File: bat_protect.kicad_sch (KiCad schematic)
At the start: 17 parts, among them Q6 Q_NMOS_DGS, Q7 Q_NMOS_DGS, Q8 Q_NMOS_DGS, U16 BQ29209DRBR

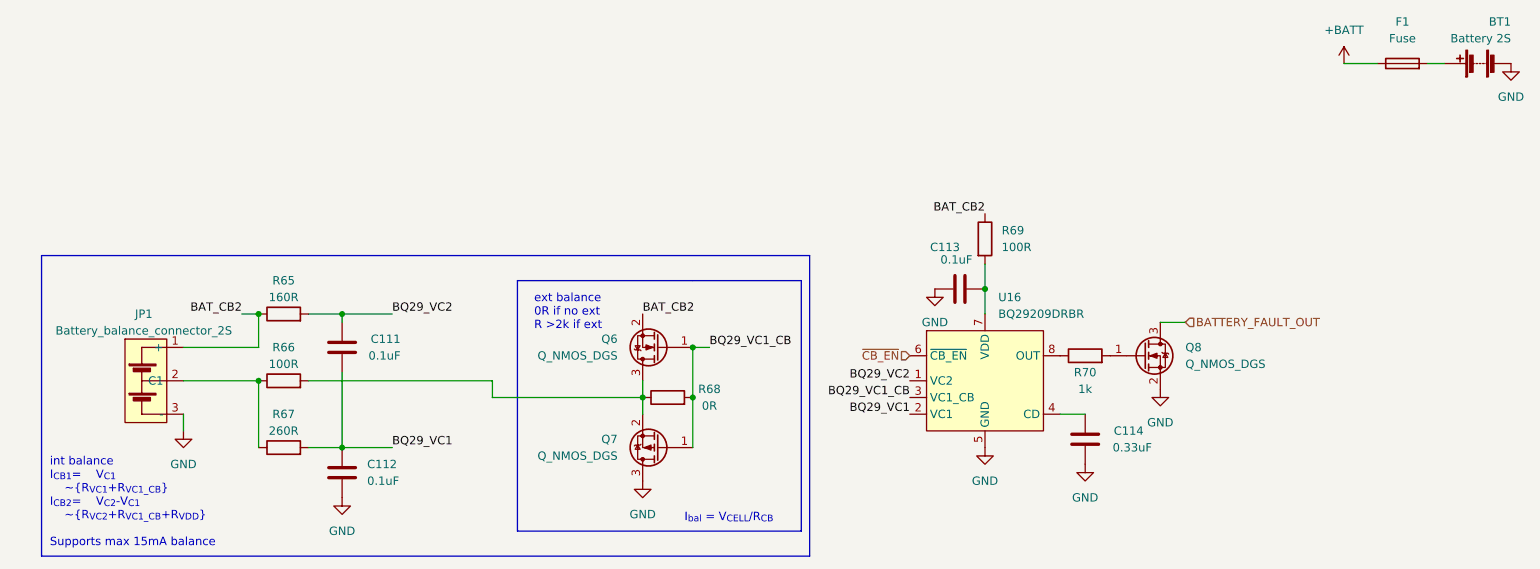
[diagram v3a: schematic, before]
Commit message: copied own LED footprint, modified silkscreen, minor visual changes in schematics
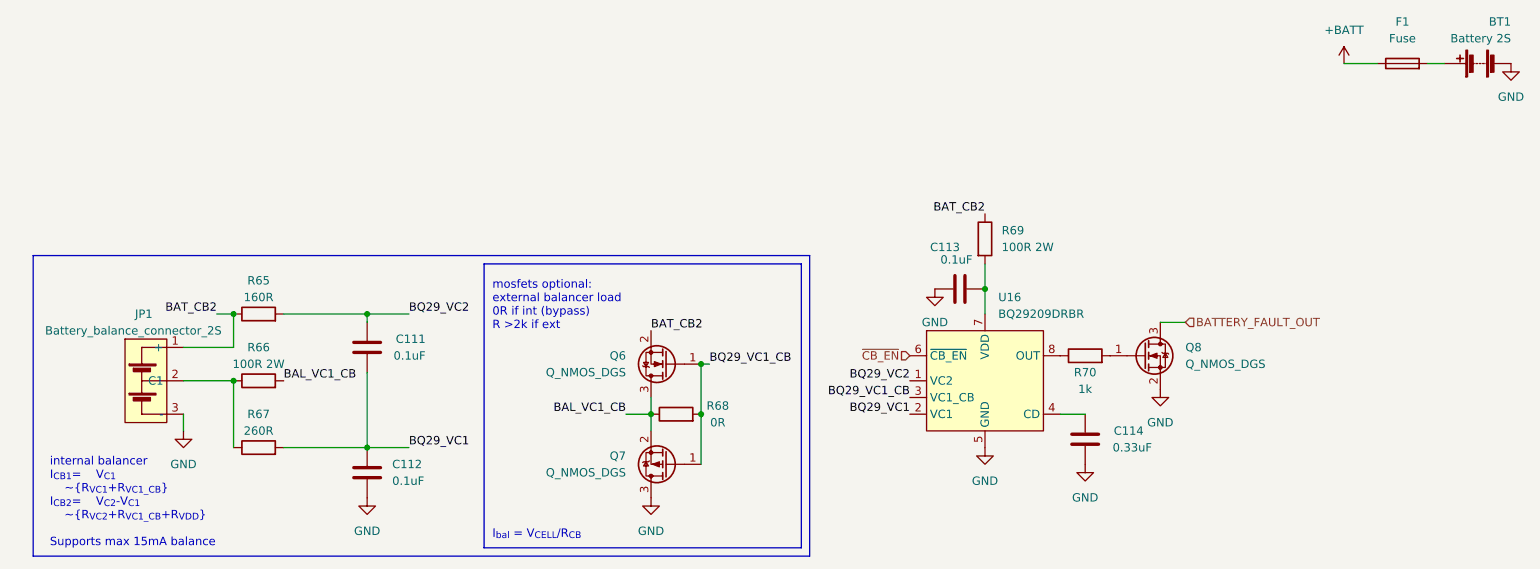
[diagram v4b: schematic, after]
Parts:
- R66, R69: value 100R -> 100R 2W
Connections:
- net BAL_VC1_CB: now reaches Q6.3 (D), Q7.2 (S), R66.2, R68.1
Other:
- note added: "internal balancer I_{CB1}= V_{C1} ~{R_{VC1}+R_{VC1_CB}} I_{CB2}= V_{C2}-V_{C1} ~{R_{VC2}+R_{VC1_CB}+R_{VDD}} Supports max 15mA balance"
- note added: "mosfets optional: external balancer load 0R if int (bypass) R >2k if ext"
- note removed: "ext balance 0R if no ext R >2k if ext"
- note removed: "int balance I_{CB1}= V_{C1} ~{R_{VC1}+R_{VC1_CB}} I_{CB2}= V_{C2}-V_{C1} ~{R_{VC2}+R_{VC1_CB}+R_{VDD}} Supports max 15mA balance"
- moved on the sheet: C111, C112, Q6, Q7, R65, R66, R67, R68

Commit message: final pcb check and minor fixes
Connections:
- net GND: now also JP1.4 (SHIELD)
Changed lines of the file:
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@@
 (kicad_sch (version 20211123) (generator eeschema)
   (paper "A4")
+  (junction (at 46.99 99.06) (diameter 0) (color 0 0 0 0)
+  )
   (junction (at 74.93 80.01) (diameter 0) (color 0 0 0 0)
   )
@@
     (stroke (width 0) (type default) (color 0 0 0 0))
   )
+  (wire (pts (xy 36.83 99.06) (xy 46.99 99.06))
+    (stroke (width 0) (type default) (color 0 0 0 0))
+  )
   (polyline (pts (xy 142.24 116.84) (xy 24.13 116.84))
     (stroke (width 0) (type default) (color 0 0 0 0))
@@
     (stroke (width 0) (type default) (color 0 0 0 0))
   )
-  (wire (pts (xy 46.99 97.79) (xy 46.99 95.25))
+  (wire (pts (xy 46.99 99.06) (xy 46.99 95.25))
     (stroke (width 0) (type default) (color 0 0 0 0))
   )
@@
     (effects (font (size 1.27 1.27)) (justify right))
   )
-  (symbol (lib_id "power:GND") (at 46.99 97.79 0) (unit 1)
-    (in_bom yes) (on_board yes) (fields_autoplaced)
-    (property "Reference" "#PWR0137" (id 0) (at 46.99 104.14 0)
-      (effects (font (size 1.27 1.27)) hide)
-    )
-    (property "Value" "GND" (id 1) (at 46.99 102.87 0))
-    (property "Footprint" "" (id 2) (at 46.99 97.79 0)
-      (effects (font (size 1.27 1.27)) hide)
-    )
-    (property "Datasheet" "" (id 3) (at 46.99 97.79 0)
+  (symbol (lib_id "power:GND") (at 46.99 99.06 0) (unit 1)
+    (in_bom yes) (on_board yes) (fields_autoplaced)
+    (property "Reference" "#PWR0137" (id 0) (at 46.99 105.41 0)
+      (effects (font (size 1.27 1.27)) hide)
+    )
+    (property "Value" "GND" (id 1) (at 46.99 104.14 0))
+    (property "Footprint" "" (id 2) (at 46.99 99.06 0)
+      (effects (font (size 1.27 1.27)) hide)
+    )
+    (property "Datasheet" "" (id 3) (at 46.99 99.06 0)
       (effects (font (size 1.27 1.27)) hide)
     )
@@
     (pin "1")
   )
-  (symbol (lib_id "airsoft_controller:Battery_balance_connector_2S") (at 40.64 90.17 0) (unit 1)
+  (symbol (lib_id "airsoft_controller:Battery_balance_connector_2S") (at 39.37 90.17 0) (unit 1)
     (in_bom yes) (on_board yes)
-    (property "Reference" "JP1" (id 0) (at 40.9575 80.01 0))
-    (property "Value" "Battery_balance_connector_2S" (id 1) (at 39.37 82.55 0))
-    (property "Footprint" "airsoft_controller:JST_XH_3P-Horizontal" (id 2) (at 40.64 90.17 0)
-      (effects (font (size 1.27 1.27)) hide)
-    )
-    (property "Datasheet" "" (id 3) (at 40.64 90.17 0)
+    (property "Reference" "JP1" (id 0) (at 39.6875 80.01 0))
+    (property "Value" "Battery_balance_connector_2S" (id 1) (at 38.1 82.55 0))
+    (property "Footprint" "airsoft_controller:JST_XH_3P-Horizontal" (id 2) (at 39.37 90.17 0)
+      (effects (font (size 1.27 1.27)) hide)
+    )
+    (property "Datasheet" "" (id 3) (at 39.37 90.17 0)
       (effects (font (size 1.27 1.27)) hide)
     )
     (pin "2")
+    (pin "4")
     (pin "1")
     (pin "3")
